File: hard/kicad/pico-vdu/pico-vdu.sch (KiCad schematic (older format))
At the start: 43 parts, among them J1 OUT, Q1 BC548, Q2 BC548, U1 65C02, U10 74HC21, U11 74HC32, U12 74HC166, U13 74HC14, U2 74HC138, U3 74HC245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

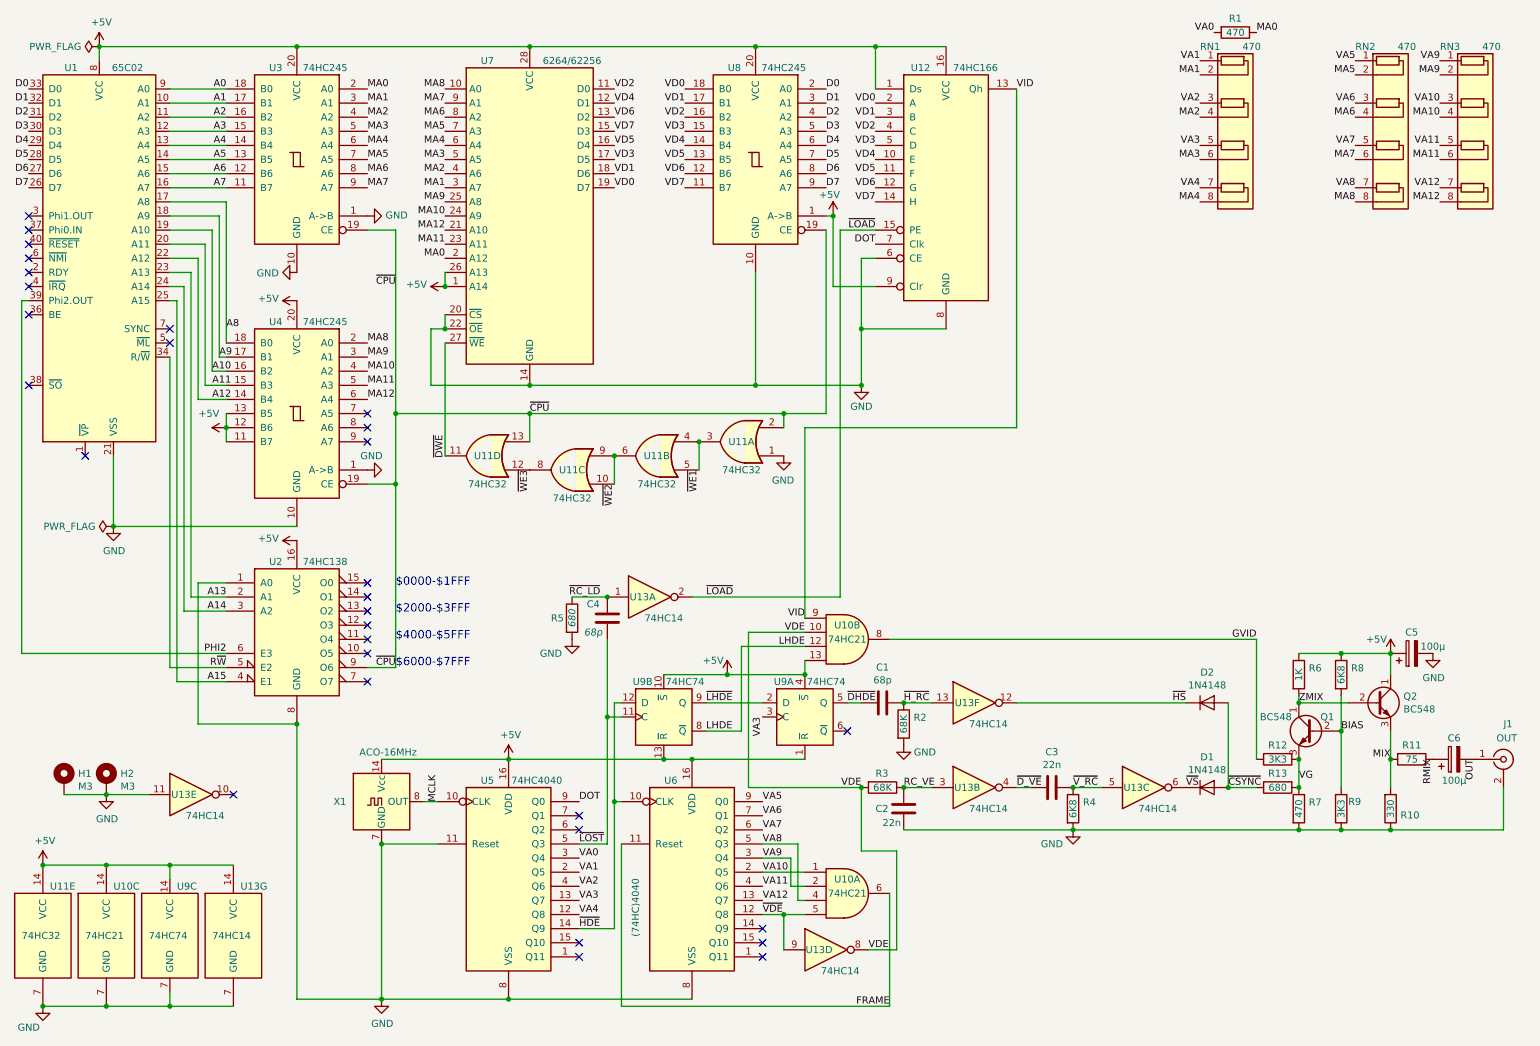
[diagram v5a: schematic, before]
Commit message: finish silkscreen for pico-VDU
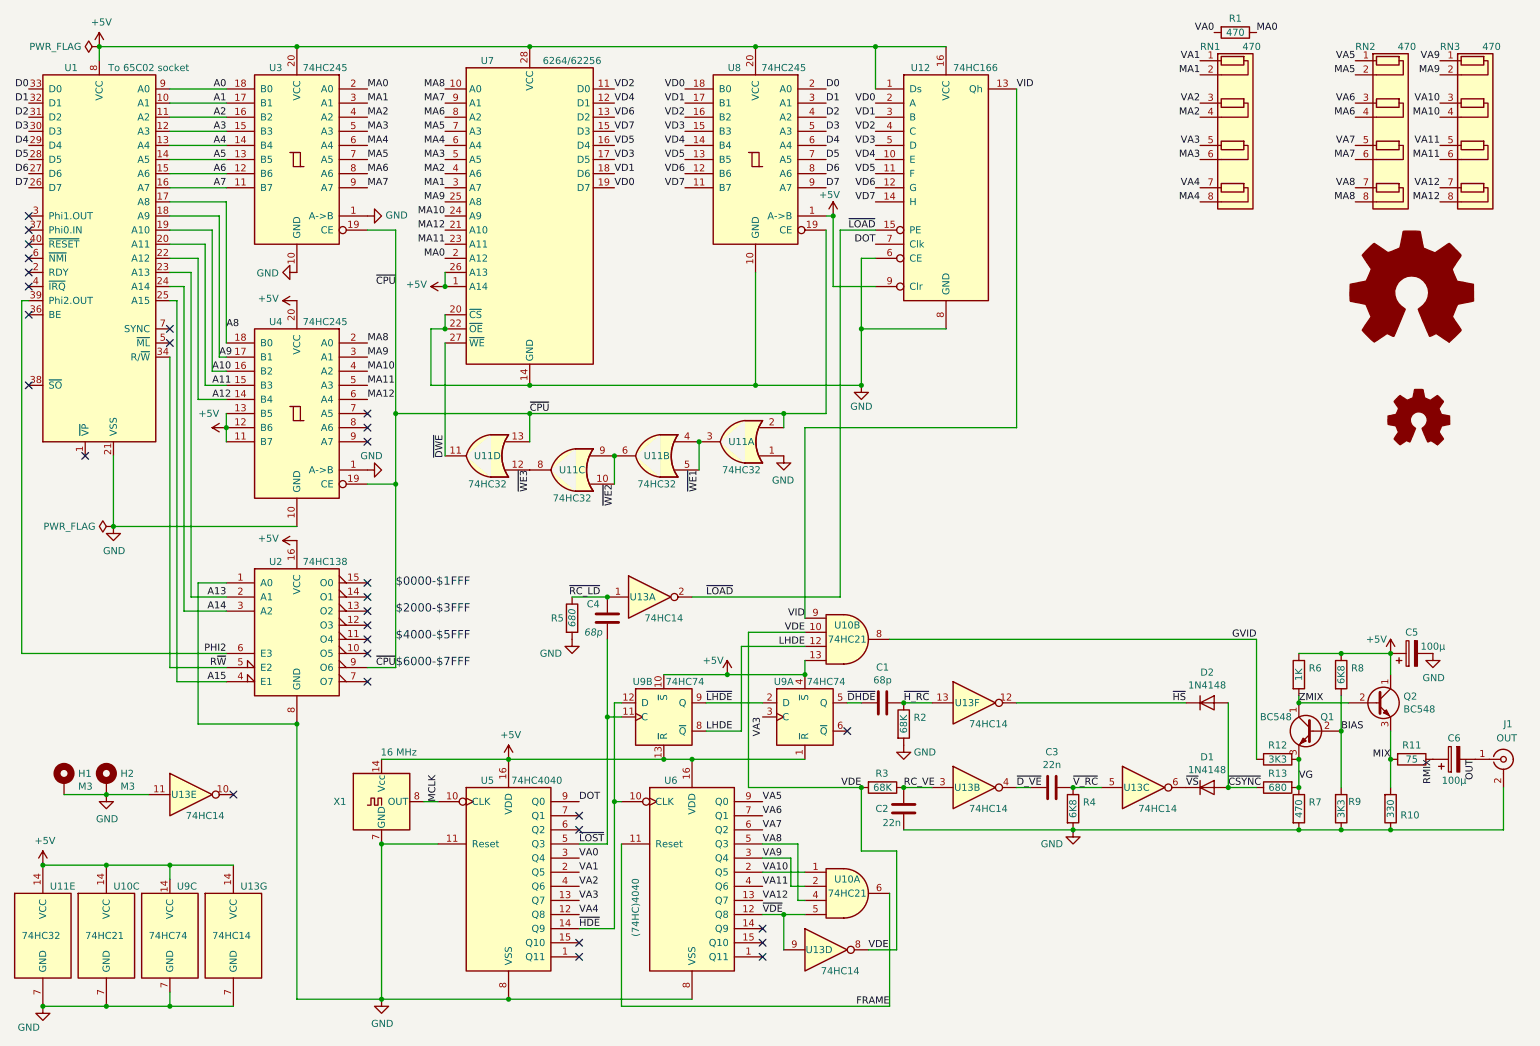
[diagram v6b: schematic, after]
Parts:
- added LOGO1: Logo_Open_Hardware_Large, Symbol:OSHW-Symbol_8.9x8mm_SilkScreen, symbol Graphic:Logo_Open_Hardware_Large
- added LOGO2: La Jaquería, durango:jaqueria, symbol Graphic:Logo_Open_Hardware_Small
- U1: value 65C02 -> To 65C02 socket
- X1: value ACO-16MHz -> 16 MHz
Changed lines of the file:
@@
 P 1150 2300
 F 0 "U1" H 950 3650 50  0000 C CNN
-F 1 "65C02" H 1350 3650 50  0000 C CNN
+F 1 "To 65C02 socket" H 1500 3650 50  0000 C CNN
 F 2 "Package_DIP:DIP-40_W15.24mm_Socket" H 1150 800 50  0001 C CNN
 F 3 "https://www.westerndesigncenter.com/wdc/documentation/w65c02s.pdf" H 1150 2300 50  0001 C CNN
@@
 P 3150 6150
 F 0 "X1" H 2900 6150 50  0000 R CNN
-F 1 "ACO-16MHz" H 3400 6500 50  0000 R CNN
+F 1 "16 MHz" H 3400 6500 50  0000 R CNN
 F 2 "Oscillator:Oscillator_DIP-14" H 3600 5800 50  0001 C CNN
 F 3 "http://www.conwin.com/datasheets/cx/cx030.pdf" H 3050 6150 50  0001 C CNN
@@
 Text Label 10900 5850 3    50   ~ 0
 OUT
+$Comp
+L Graphic:Logo_Open_Hardware_Large LOGO1
+U 1 1 661705D4
+P 10450 2550
+F 0 "LOGO1" H 10450 3050 50  0001 C CNN
+F 1 "Logo_Open_Hardware_Large" H 10450 2150 50  0001 C CNN
+F 2 "Symbol:OSHW-Symbol_8.9x8mm_SilkScreen" H 10450 2550 50  0001 C CNN
+F 3 "~" H 10450 2550 50  0001 C CNN
+	1    10450 2550
+	1    0    0    -1
+$EndComp
+$Comp
+L Graphic:Logo_Open_Hardware_Small LOGO2
+U 1 1 66171AA6
+P 10500 3450
+F 0 "LOGO2" H 10500 3725 50  0001 C CNN
+F 1 "La Jaquería" H 10500 3225 50  0001 C CNN
+F 2 "durango:jaqueria" H 10500 3450 50  0001 C CNN
+F 3 "~" H 10500 3450 50  0001 C CNN
+	1    10500 3450
+	1    0    0    -1
+$EndComp
 $EndSCHEMATC

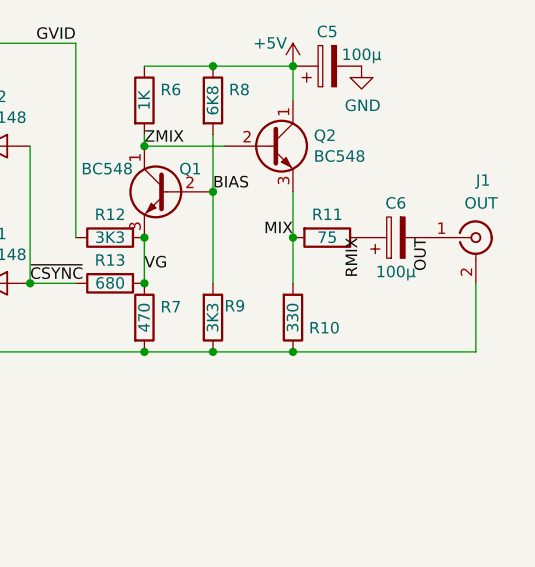
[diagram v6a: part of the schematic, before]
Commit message: add RCA footprint
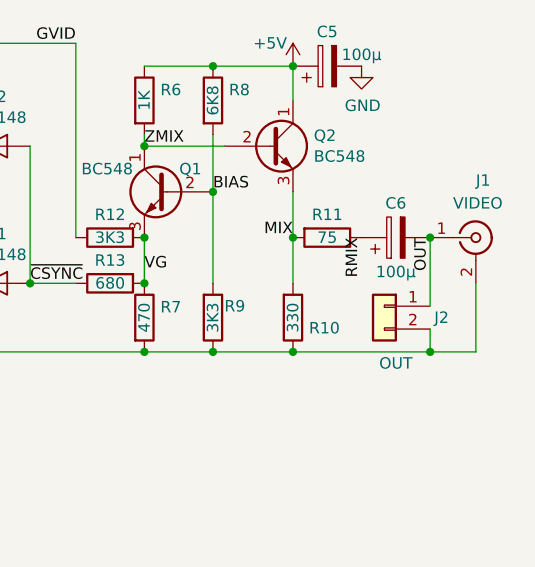
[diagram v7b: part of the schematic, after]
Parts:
- added J2: OUT, Connector_PinSocket_2.54mm:PinSocket_1x02_P2.54mm_Horizontal, symbol Connector_Generic:Conn_01x02
- J1: value OUT -> VIDEO; footprint Connector_PinSocket_2.54mm:PinSocket_1x02_P2.54mm_Horizontal -> durango:1xRCA
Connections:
- net GND: now also J2.2 (Pin_2)
- net OUT: now also J2.1 (Pin_1)
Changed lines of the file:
@@
 P 11100 5850
 F 0 "J1" H 11100 6100 50  0000 L CNN
-F 1 "OUT" H 11050 6000 50  0000 L CNN
-F 2 "Connector_PinSocket_2.54mm:PinSocket_1x02_P2.54mm_Horizontal" H 11100 5850 50  0001 C CNN
+F 1 "VIDEO" H 11000 6000 50  0000 L CNN
+F 2 "durango:1xRCA" H 11100 5850 50  0001 C CNN
 F 3 " ~" H 11100 5850 50  0001 C CNN
 	1    11100 5850
@@
 	11100 6050 11100 6350
 Wire Wire Line
-	11100 6350 10300 6350
+	11100 6350 10900 6350
 Connection ~ 10300 6350
 Text Label 10900 5850 3    50   ~ 0
@@
 	1    0    0    -1
 $EndComp
+Wire Wire Line
+	10900 5850 10900 6150
+Connection ~ 10900 5850
+$Comp
+L Connector_Generic:Conn_01x02 J2
+U 1 1 660A2305
+P 10700 6150
+F 0 "J2" H 10450 6100 50  0000 C CNN
+F 1 "OUT" H 10650 5900 50  0000 C CNN
+F 2 "Connector_PinSocket_2.54mm:PinSocket_1x02_P2.54mm_Horizontal" H 10700 6150 50  0001 C CNN
+F 3 "~" H 10700 6150 50  0001 C CNN
+	1    10700 6150
+	-1   0    0    -1
+$EndComp
+Wire Wire Line
+	10900 6250 10900 6350
+Connection ~ 10900 6350
+Wire Wire Line
+	10900 6350 10300 6350
 $EndSCHEMATC

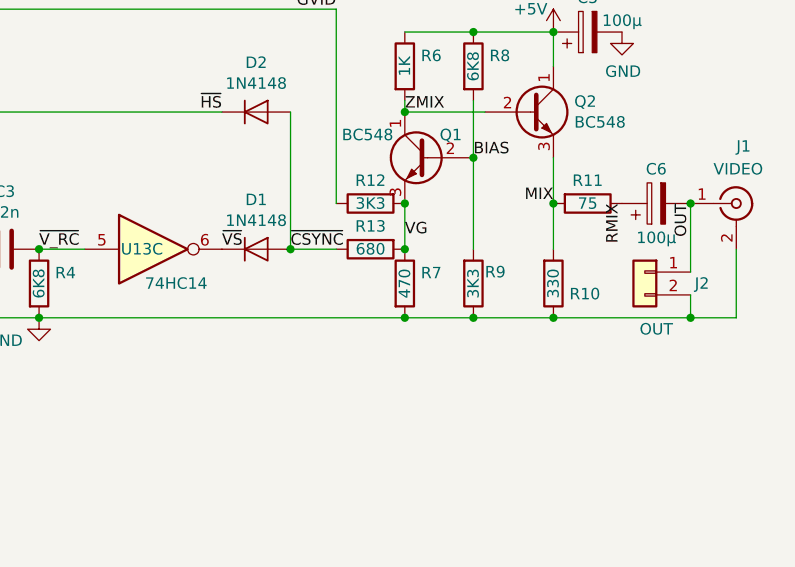
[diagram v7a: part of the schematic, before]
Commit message: fix Chihuaha via sizes
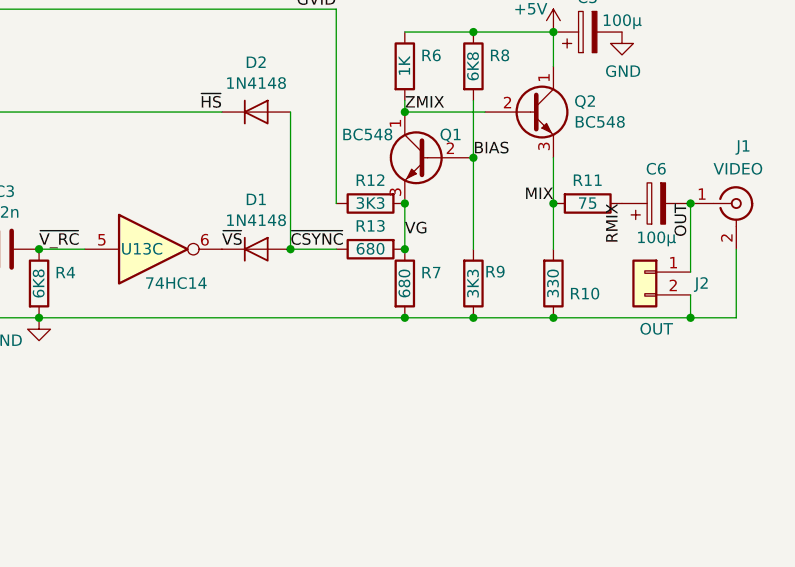
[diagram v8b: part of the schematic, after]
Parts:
- R7: value 470 -> 680
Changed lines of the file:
@@
 P 9650 6200
 F 0 "R7" H 9720 6246 50  0000 L CNN
-F 1 "470" V 9650 6200 50  0000 C CNN
+F 1 "680" V 9650 6200 50  0000 C CNN
 F 2 "Resistor_THT:R_Axial_DIN0207_L6.3mm_D2.5mm_P2.54mm_Vertical" V 9580 6200 50  0001 C CNN
 F 3 "~" H 9650 6200 50  0001 C CNN
